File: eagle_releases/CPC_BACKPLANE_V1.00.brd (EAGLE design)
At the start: 100.3 x 81.3 mm, 11 parts

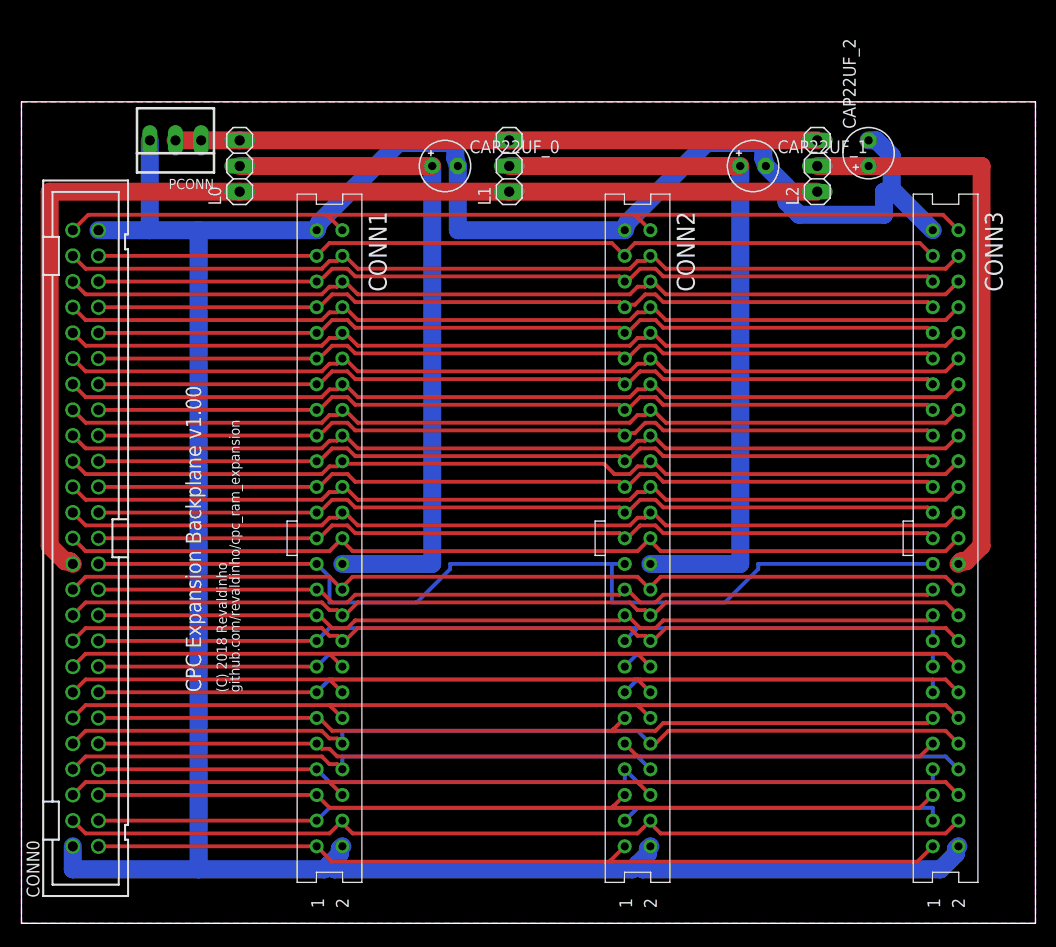
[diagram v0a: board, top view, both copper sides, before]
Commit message: Minor trim of CPC_BACKPLANE Board size to fit Seeed 100x100mm limit
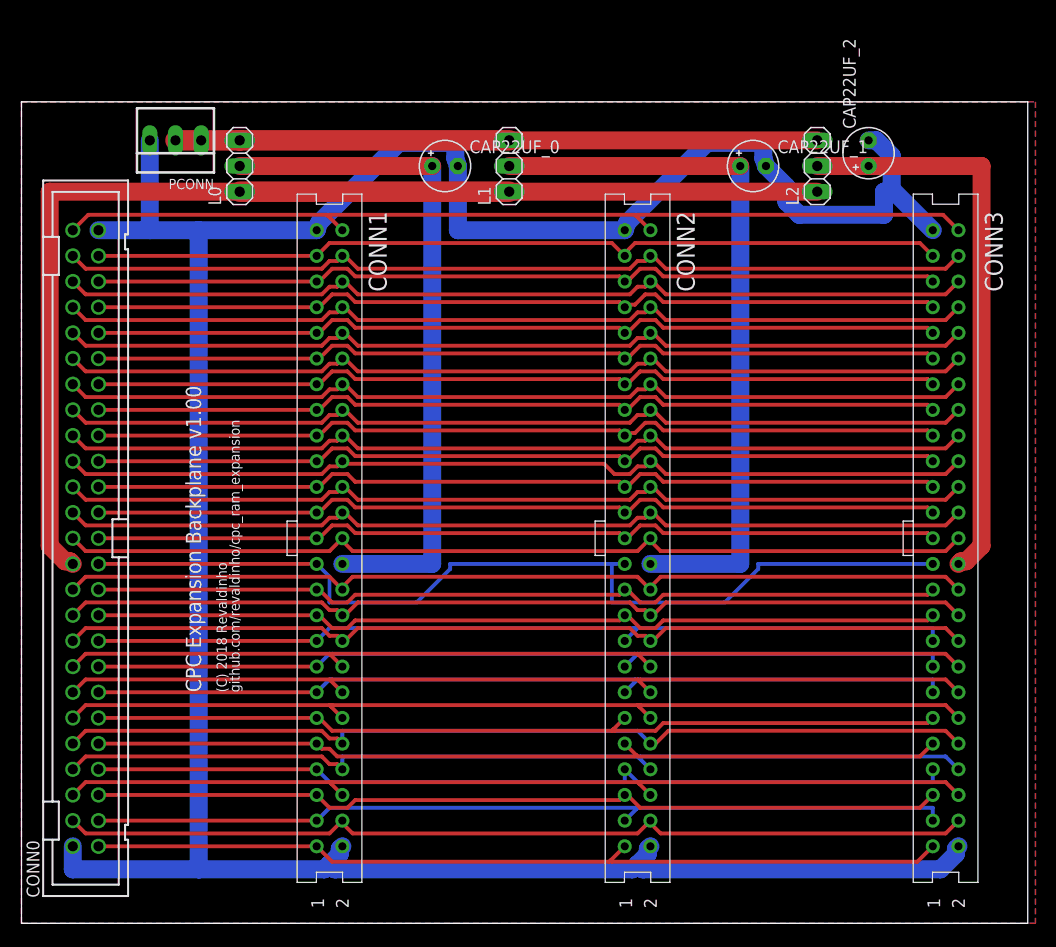
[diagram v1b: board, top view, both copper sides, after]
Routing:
- net CURSOR: track 85.3 -> 84.8 mm
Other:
- board size 100.3 x 81.3 mm -> 99.6 x 81.3 mm
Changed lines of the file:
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@@
 <board>
 <plain>
-<wire x1="0" y1="0" x2="100.33" y2="0" width="0" layer="20"/>
-<wire x1="100.33" y1="0" x2="100.33" y2="81.28" width="0" layer="20"/>
-<wire x1="100.33" y1="81.28" x2="0" y2="81.28" width="0" layer="20"/>
+<wire x1="0" y1="0" x2="99.568" y2="0" width="0" layer="20"/>
+<wire x1="99.568" y1="0" x2="99.568" y2="81.28" width="0" layer="20"/>
+<wire x1="99.568" y1="81.28" x2="0" y2="81.28" width="0" layer="20"/>
 <wire x1="0" y1="81.28" x2="0" y2="0" width="0" layer="20"/>
 <text x="17.78" y="22.86" size="1.524" layer="21" rot="R90">CPC Expansion Backplane v1.00</text>
@@
 <wire x1="2.794" y1="72.39" x2="2.794" y2="37.338" width="1.778" layer="1"/>
 <wire x1="21.59" y1="72.39" x2="2.794" y2="72.39" width="1.778" layer="1"/>
-<wire x1="48.26" y1="72.39" x2="21.59" y2="72.39" width="1.778" layer="1"/>
+<wire x1="48.26" y1="72.39" x2="21.59" y2="72.39" width="2.032" layer="1"/>
 </signal>
 <signal name="A2">
@@
 <contactref element="CONN3" pad="5"/>
 <wire x1="7.62" y1="12.7" x2="29.21" y2="12.7" width="0.381" layer="1"/>
-<wire x1="58.42" y1="11.43" x2="58.547" y2="11.557" width="0.381" layer="1"/>
-<wire x1="58.547" y1="11.557" x2="59.69" y2="12.7" width="0.381" layer="1"/>
-<wire x1="30.48" y1="11.43" x2="58.42" y2="11.43" width="0.381" layer="1"/>
+<wire x1="59.182" y1="12.192" x2="59.69" y2="12.7" width="0.381" layer="1"/>
+<wire x1="33.02" y1="12.192" x2="59.182" y2="12.192" width="0.381" layer="1"/>
+<wire x1="32.258" y1="11.43" x2="33.02" y2="12.192" width="0.381" layer="1"/>
+<wire x1="30.48" y1="11.43" x2="32.258" y2="11.43" width="0.381" layer="1"/>
 <wire x1="29.21" y1="12.7" x2="30.48" y2="11.43" width="0.381" layer="1"/>
 <wire x1="88.9" y1="11.43" x2="90.17" y2="12.7" width="0.381" layer="1"/>
-<wire x1="58.674" y1="11.43" x2="88.9" y2="11.43" width="0.381" layer="1"/>
-<wire x1="58.674" y1="11.43" x2="58.547" y2="11.557" width="0.381" layer="1"/>
+<wire x1="61.214" y1="11.43" x2="88.9" y2="11.43" width="0.381" layer="1"/>
+<wire x1="60.198" y1="12.446" x2="61.214" y2="11.43" width="0.381" layer="1"/>
+<wire x1="59.69" y1="12.446" x2="60.198" y2="12.446" width="0.381" layer="1"/>
+<wire x1="59.69" y1="12.446" x2="59.69" y2="12.7" width="0.381" layer="1"/>
 </signal>
 <signal name="VDD" class="1">
@@
 <vertex x="0" y="0"/>
 <vertex x="0" y="81.28"/>
+<vertex x="99.568" y="81.28"/>
 <vertex x="100.33" y="81.28"/>
 <vertex x="100.33" y="0"/>
@@
 <vertex x="0" y="0"/>
 <vertex x="0" y="81.28"/>
+<vertex x="99.568" y="81.28"/>
 <vertex x="100.33" y="81.28"/>
 <vertex x="100.33" y="0"/>
@@
 <contactref element="PCONN" pad="1"/>
 <wire x1="48.26" y1="77.47" x2="78.74" y2="77.47" width="1.778" layer="1"/>
-<wire x1="15.24" y1="77.47" x2="17.78" y2="77.47" width="1.778" layer="1"/>
-<wire x1="17.78" y1="77.47" x2="21.59" y2="77.47" width="1.778" layer="1"/>
-<wire x1="21.59" y1="77.47" x2="48.26" y2="77.47" width="1.778" layer="1"/>
+<wire x1="15.24" y1="77.47" x2="17.78" y2="77.47" width="2.032" layer="1"/>
+<wire x1="17.78" y1="77.47" x2="21.59" y2="77.47" width="2.032" layer="1"/>
+<wire x1="21.59" y1="77.47" x2="48.26" y2="77.47" width="2.032" layer="1"/>
 </signal>
 <signal name="D6">

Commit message: Update cpc_backplane PCB
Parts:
- moved CONN1 1.80 mm to (31.8, 36.8)
- moved CAP22UF_0 1.27 mm to (43.2, 74.9)
- moved CONN0 1.27 mm to (6.35, 36.8)
- moved CONN2 1.27 mm to (61.0, 36.8)
- moved CONN3 1.27 mm to (91.4, 36.8)
- moved L1 1.27 mm to (49.5, 74.9)
- moved L0 1.27 mm to (22.9, 74.9)
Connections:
- net VDD renamed VDD1
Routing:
- net VSS: track 282.5 -> 286.1 mm
- net VDD_CPC: track 114.0 -> 115.3 mm
- net VDD3: track 56.9 -> 58.1 mm
- net VDD1: track 67.3 -> 68.6 mm
- net RAMRD_B: track 86.1 -> 85.3 mm
- net NMI_B: track 86.1 -> 85.3 mm
- net BUSACK_B: track 86.1 -> 85.3 mm
- net HALT_B: track 86.1 -> 85.3 mm
- net ROMDIS: track 92.2 -> 91.5 mm
- net READY: track 92.1 -> 91.5 mm
- net RAMDIS: track 92.1 -> 91.5 mm
- net BUSRQ_B: track 92.1 -> 91.5 mm
- net RFSH_B: track 84.8 -> 85.3 mm

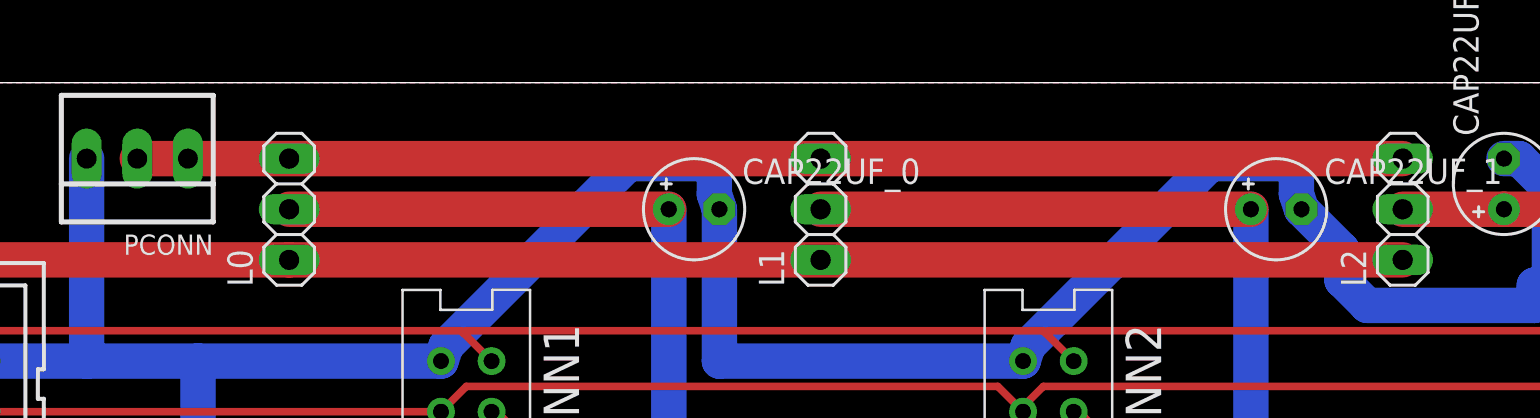
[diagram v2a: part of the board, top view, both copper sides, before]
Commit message: Minor board updates for backplane and 74 series RAM exp ; update utils
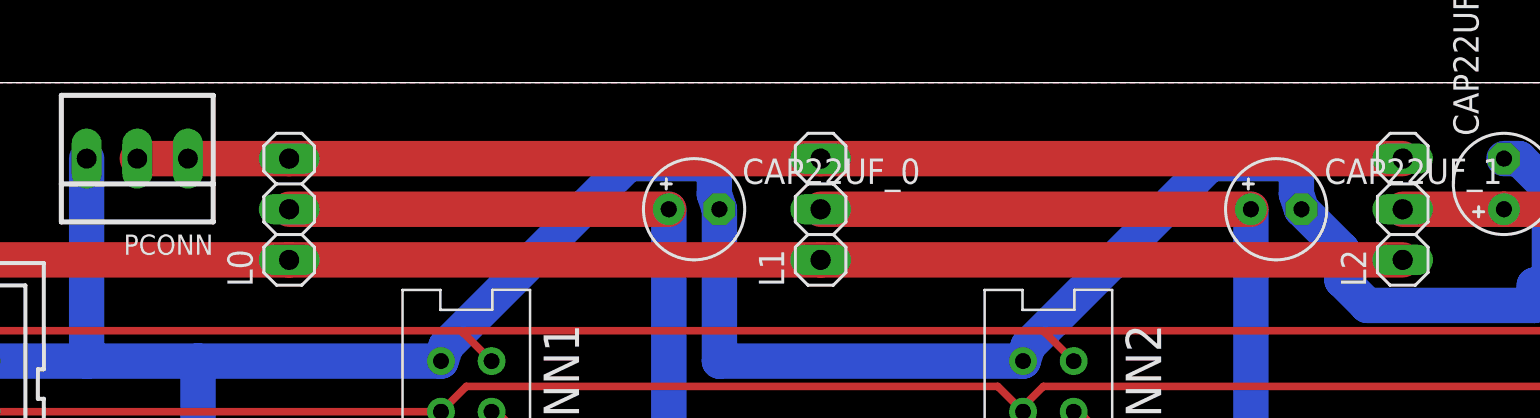
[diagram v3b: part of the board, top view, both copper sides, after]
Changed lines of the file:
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@@
 <contactref element="L2" pad="1"/>
 <contactref element="CONN0" pad="24"/>
-<wire x1="22.86" y1="72.39" x2="78.74" y2="72.39" width="1.778" layer="1"/>
+<wire x1="22.86" y1="72.39" x2="49.53" y2="72.39" width="1.778" layer="1"/>
+<wire x1="49.53" y1="72.39" x2="78.74" y2="72.39" width="1.778" layer="1"/>
 <wire x1="4.826" y1="34.544" x2="5.08" y2="34.29" width="1.778" layer="1"/>
 <wire x1="4.318" y1="34.544" x2="4.826" y2="34.544" width="1.778" layer="1"/>
@@
 <wire x1="2.794" y1="72.39" x2="2.794" y2="36.068" width="1.778" layer="1"/>
 <wire x1="22.86" y1="72.39" x2="2.794" y2="72.39" width="1.778" layer="1"/>
-<wire x1="22.86" y1="72.39" x2="49.53" y2="72.39" width="0" layer="19" extent="1-1"/>
 </signal>
 <signal name="A2">
@@
 <contactref element="PCONN" pad="2"/>
 <contactref element="PCONN" pad="1"/>
-<wire x1="15.24" y1="77.47" x2="78.74" y2="77.47" width="1.778" layer="1"/>
-<wire x1="22.86" y1="77.47" x2="49.53" y2="77.47" width="0" layer="19" extent="1-1"/>
-<wire x1="17.78" y1="77.47" x2="22.86" y2="77.47" width="0" layer="19" extent="1-1"/>
-<wire x1="15.24" y1="77.47" x2="17.78" y2="77.47" width="0" layer="19" extent="1-1"/>
+<wire x1="15.24" y1="77.47" x2="17.78" y2="77.47" width="1.778" layer="1"/>
+<wire x1="17.78" y1="77.47" x2="22.86" y2="77.47" width="1.778" layer="1"/>
+<wire x1="22.86" y1="77.47" x2="49.53" y2="77.47" width="1.778" layer="1"/>
+<wire x1="49.53" y1="77.47" x2="78.74" y2="77.47" width="1.778" layer="1"/>
 </signal>
 <signal name="VDD1" class="1">
